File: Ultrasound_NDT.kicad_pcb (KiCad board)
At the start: 6 copper layers, 100 x 100 mm, 316 parts, among them J1 Conn_01x02_Pin, J10 CONSMA002-SMD, J11 Logger Connector, J12 UART Connector, J13 External UART, J14 External I2C, J15 JTAG Header, J16 Conn_02x04_Odd_Even, J17 Input Power, J18 Conn_01x02_Pin, J19 Conn_01x02_Pin, J2 Conn_01x02_Pin, J20 Conn_01x02_Pin, J21 Conn_01x02_Pin, J22 Conn_01x02_Pin, J23 Conn_01x02_Pin, J24 Conn_01x02_Pin, J25 Conn_01x02_Pin, J26 Spectrography Power, J27 Conn_01x02_Pin, J28 Conn_02x04_Odd_Even, J3 CONSMA002-SMD, J4 CONSMA002-SMD, J5 CONSMA002-SMD, J6 CONSMA002-SMD, J7 CONSMA002-SMD, J8 CONSMA002-SMD, J9 CONSMA002-SMD, SW1 XRSn_button, U1 AD8334ACPZ, U10 TLV9354IDR, U11 TLV9354IDR, U12 TPS63700DRCR, U13 M24M01E-FMN6TP, U14 LDL212PU50R, U15 AZ1117CH2-3.3, U16 AZ1117CH2-3.3, U17 TRS3221EIPWR, U2 DSC1001DI2-125.0000T, U3 MAX14808ETK_, U4 AD8334ACPZ, U5 F280025PNS, U6 REF3030, U7 MIC920YC5-TR, U8 TLV9354IDR, U9 TLV9354IDR, Y2 H130B-16.000-18-3030-EXT-TR

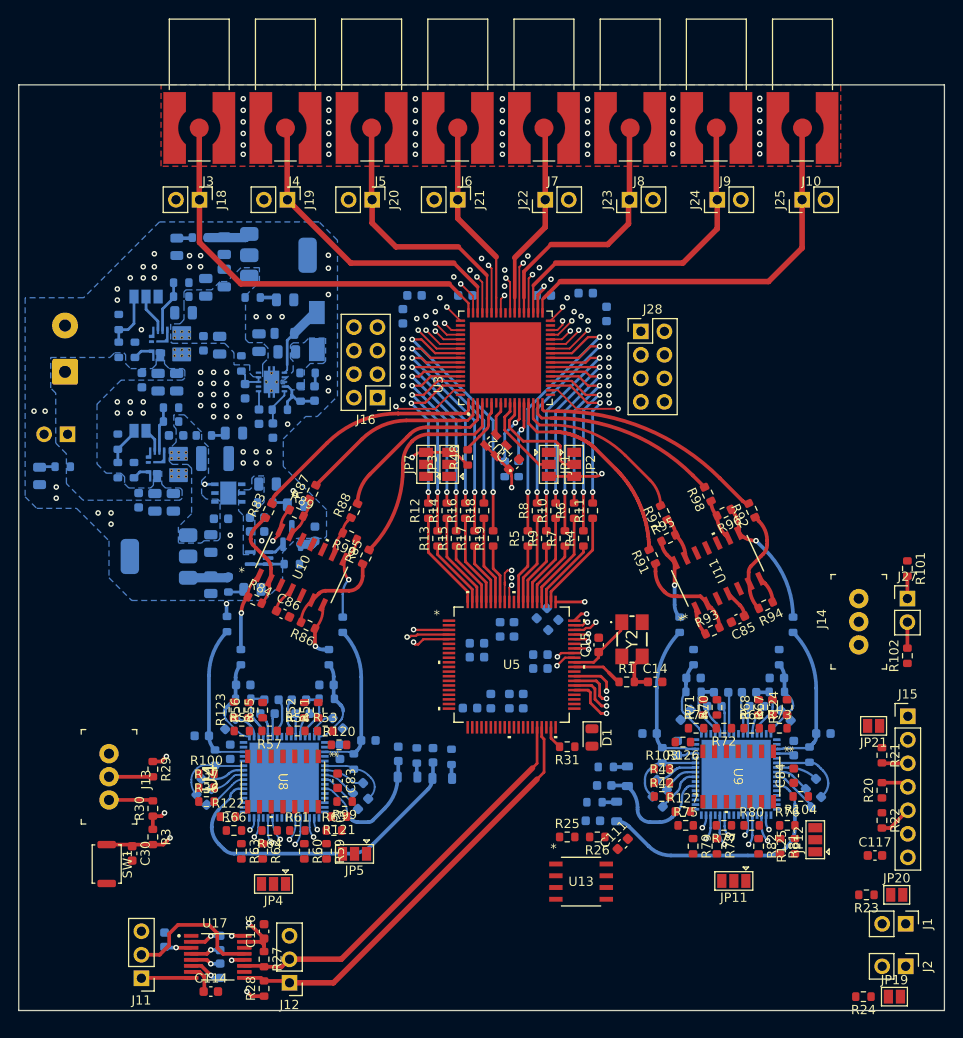
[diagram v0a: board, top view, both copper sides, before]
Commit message: Finished 70% fr this time, power planes are remaining and some minor connections to the AFE's power & cfg pins, dont forget xrst
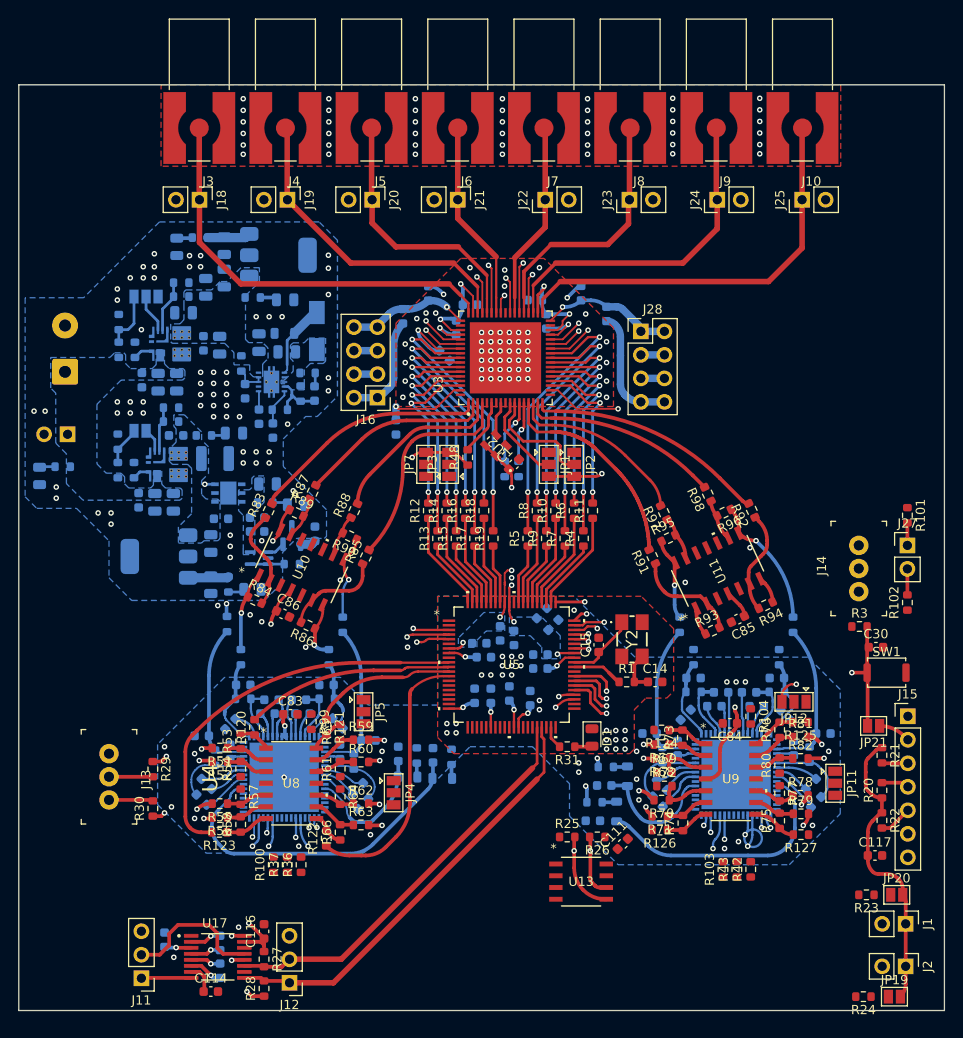
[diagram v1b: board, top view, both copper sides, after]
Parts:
- moved SW1 86.7 mm to (153.5, 98.2), turned to 0 degrees
- moved C30 83.4 mm to (152.3, 95.5), turned to 0 degrees
- moved R3 79.7 mm to (150.6, 93.3), turned to 0 degrees
- moved JP4 16.3 mm to (100.2, 111.2), turned to -90 degrees
- moved JP5 15.4 mm to (97.0, 102.5), turned to -90 degrees
- moved JP11 15.2 mm to (147.9, 110.2), turned to -90 degrees
- moved JP12 15.1 mm to (143.5, 101.4), turned to 180 degrees
- moved R124 13.8 mm to (129.2, 104.5), turned to 180 degrees
- moved R125 13.4 mm to (144.2, 103.6), turned to 180 degrees
- moved R123 13.3 mm to (81.4, 115.5), turned to 180 degrees
- moved R63 13.2 mm to (96.7, 114.7), turned to 0 degrees
- moved R127 13.0 mm to (144.2, 115.8), turned to 180 degrees
- moved R103 12.7 mm to (135.8, 119.5), turned to 90 degrees
- moved R71 12.6 mm to (129.0, 113.8), turned to 180 degrees
- moved R67 12.6 mm to (129.2, 106.0), turned to 180 degrees
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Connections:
- C37 pad 1: /Receiving Section/TR_OUT2 -> /Receiving Section/TR_OUT4
- R120 pad 2: /Main MCU Section/ADC1 -> /Main MCU Section/ADC2
- R123 pad 2: /Main MCU Section/ADC2 -> /Main MCU Section/ADC1
- R130 pad 2: /Receiving Section/TR_OUT2 -> /Receiving Section/TR_OUT4
- R33 pad 1: /Receiving Section/TR_OUT2 -> /Receiving Section/TR_OUT4
- R51 pad 2: /Receiving Section/ADC1_L -> /Receiving Section/ADC2_L
- R52 pad 2: /Receiving Section/ADC1_H -> /Receiving Section/ADC2_H
- R55 pad 2: /Receiving Section/ADC2_H -> /Receiving Section/ADC1_H
- R56 pad 2: /Receiving Section/ADC2_L -> /Receiving Section/ADC1_L
- U4 pad 16: /Receiving Section/TR_OUT2 -> /Receiving Section/TR_OUT4
- U5 pad 10: /Main MCU Section/ADC3 -> /Main MCU Section/ADC1
- U5 pad 12: /Main MCU Section/ADC1 -> /Main MCU Section/ADC4
- U5 pad 13: /Main MCU Section/ADC4 -> /Main MCU Section/ADC3
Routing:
- net /Main MCU Section/RS232_FOFF: track 61.8 -> 3.00 mm
- net /Main MCU Section/ADC1: track 0.00 -> 42.6 mm
- net MCU_IO_3V3: track 31.3 -> 72.4 mm, vias 7 -> 11
- net /Main MCU Section/XRSn: track 46.5 -> 15.6 mm
- net /Main MCU Section/ADC3: track 0.00 -> 28.6 mm
- net /Main MCU Section/I2CA_SDA: track 0.00 -> 26.9 mm, vias 0 -> 2
- net /Main MCU Section/I2CA_SCL: track 0.00 -> 26.1 mm, vias 0 -> 2
- net /Main MCU Section/ADC2: track 0.00 -> 22.6 mm
- net /Main MCU Section/AFE_GAIN_B2: track 2.68 -> 21.9 mm, vias 1 -> 2
- net /Main MCU Section/AFE_GAIN_B1: track 1.57 -> 19.2 mm, vias 1 -> 2
- net +5V: track 5.87 -> 22.7 mm, vias 0 -> 4
- net /Main MCU Section/ADC4: track 0.00 -> 15.5 mm
- net VGNB: track 2.52 -> 17.1 mm
- net /Receiving Section/ADC4_L: track 2.16 -> 16.4 mm, vias 1 -> 2
- net /Receiving Section/ADC2_H: track 2.52 -> 16.8 mm, vias 1 -> 2
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- added copper zone on In4.Cu, net GND
- added copper zone on B.Cu, net MCU_1V2
- added copper zone on B.Cu, net MCU_IO_3V3

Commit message: 1/4 AFE edits left to go, check if MCU ADC channels could be swapped (use oth ADCs), add voltage monitoring & power planes
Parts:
- moved JP4 15.1 mm to (88.1, 120.2), turned to 180 degrees
- moved JP11 11.7 mm to (142.1, 120.2), turned to 180 degrees
- moved R100 10.5 mm to (76.7, 119.0)
- moved R36 10.5 mm to (79.7, 119.0)
- moved R37 10.5 mm to (78.2, 119.0)
- moved C4 4.68 mm to (119.2, 63.0), turned to -90 degrees
- moved C78 2.22 mm to (146.5, 110.1), turned to -90 degrees
- moved C75 1.84 mm to (128.0, 110.5), turned to -90 degrees
- moved C42 1.40 mm to (97.8, 111.3), turned to -90 degrees
- moved R62 1.33 mm to (97.7, 111.5)
- moved R64 0.99 mm to (95.4, 112.0)
- moved C66 0.92 mm to (146.7, 103.9)
- moved C82 0.84 mm to (145.0, 109.5), turned to -90 degrees
- moved C57 0.83 mm to (127.9, 104.0)
- moved C84 0.77 mm to (136.6, 103.0)
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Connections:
- C63 pad 1: /Receiving Section/TR_OUT6 -> /Receiving Section/TR_OUT8
- R128 pad 2: /Receiving Section/TR_OUT6 -> /Receiving Section/TR_OUT8
- R45 pad 1: /Receiving Section/TR_OUT6 -> /Receiving Section/TR_OUT8
- U1 pad 16: /Receiving Section/TR_OUT6 -> /Receiving Section/TR_OUT8
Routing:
- net +5V: track 22.7 -> 38.1 mm, vias 4 -> 10
- net /Receiving Section/ADC2_H: track 16.8 -> 4.77 mm
- net /Receiving Section/ADC2_L: track 14.6 -> 2.78 mm
- net /Receiving Section/MODE_B: track 0.00 -> 9.13 mm, vias 0 -> 1
- net /Receiving Section/TR_OUT6: track 25.7 -> 16.6 mm
- net /Receiving Section/TR_OUT8: track 0.00 -> 8.84 mm
- net /Receiving Section/ADC1_H: track 11.1 -> 3.97 mm
- net /Receiving Section/MODE_A: track 0.00 -> 6.49 mm, vias 0 -> 1
- net /Receiving Section/ADC1_L: track 10.5 -> 4.15 mm
- net Net-(U9-+IN_B): track 5.78 -> 0.00 mm
- net /Receiving Section/ADC8_L: track 14.5 -> 18.8 mm
- net /Receiving Section/HILO_B: track 0.00 -> 3.80 mm, vias 0 -> 1
- net Net-(U1-LMD3): track 0.00 -> 3.17 mm
- net /Receiving Section/HILO_A: track 0.00 -> 3.04 mm, vias 0 -> 1
- net /Receiving Section/LNAA8_N: track 8.55 -> 6.11 mm
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
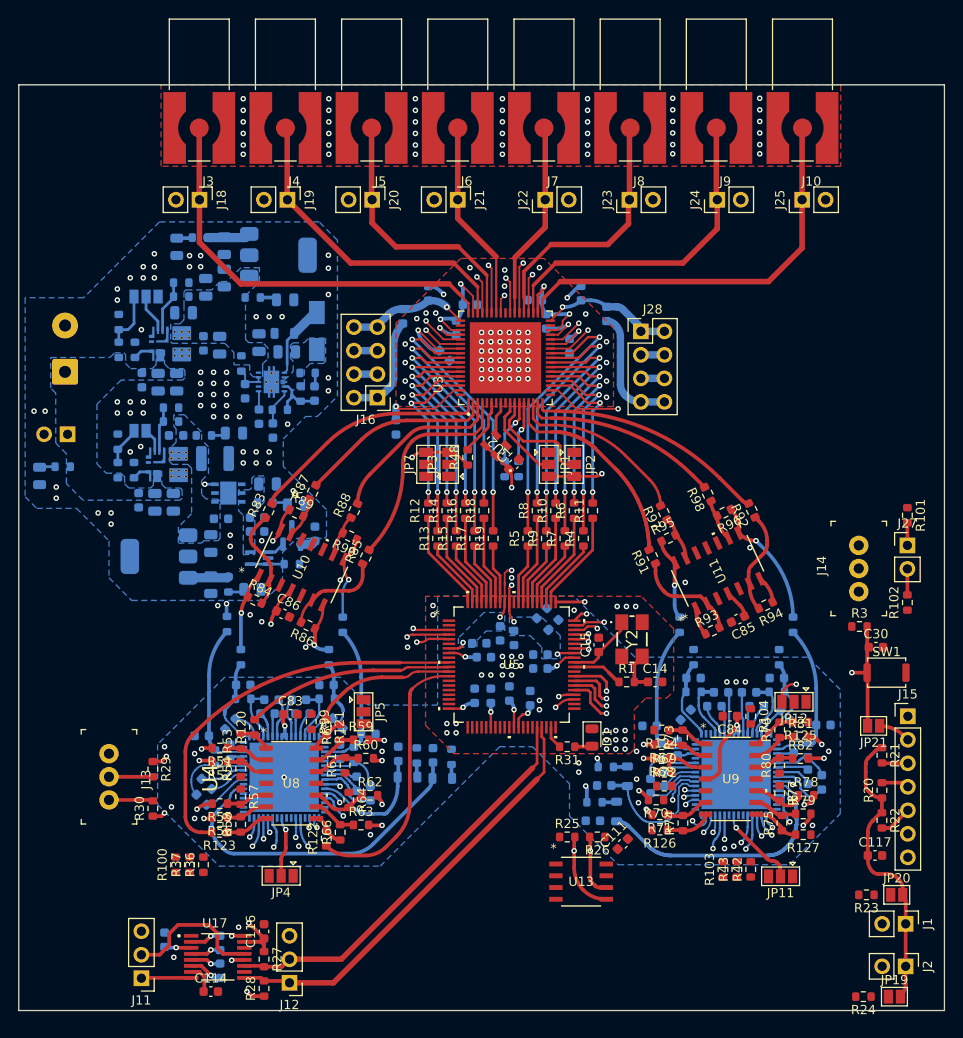
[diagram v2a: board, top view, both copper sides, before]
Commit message: 5% left, rearrange ADC channels for right AFE
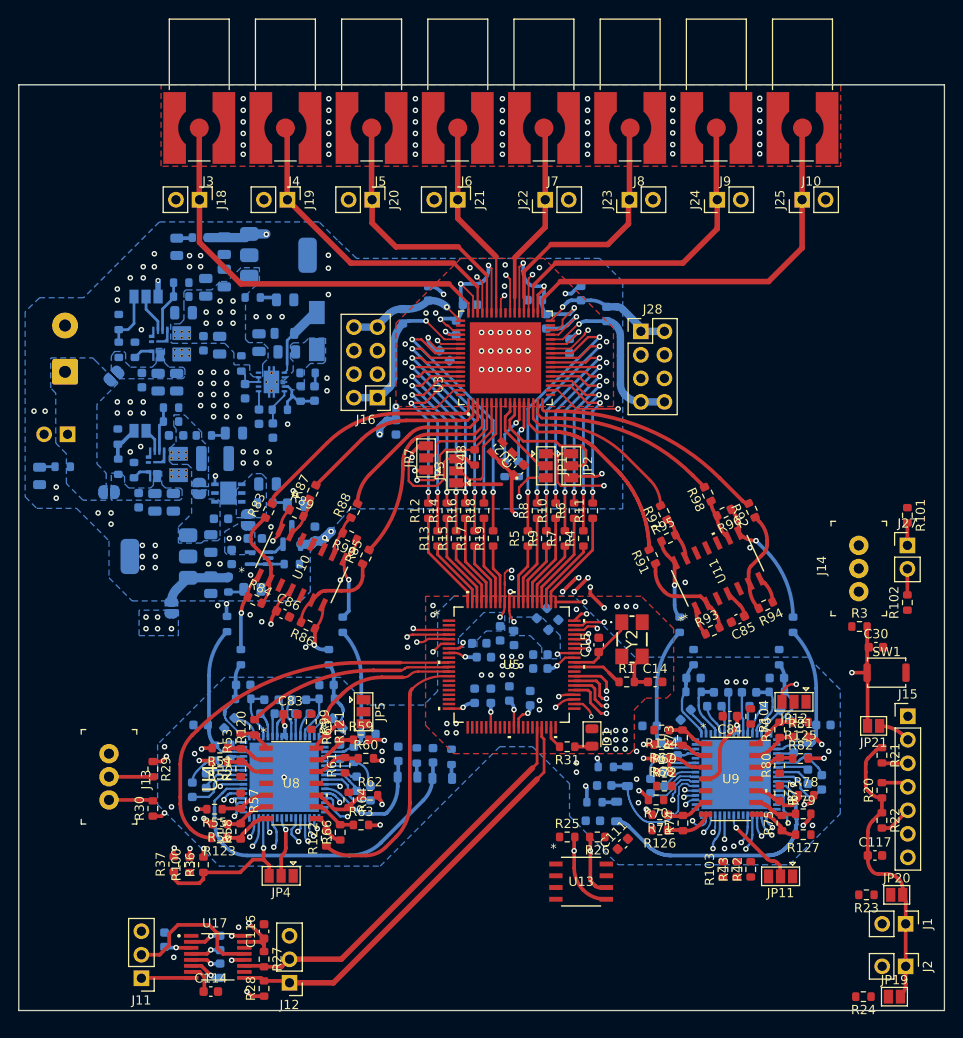
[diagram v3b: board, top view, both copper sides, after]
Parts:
- added JP10: SolderJumper_2_Open, Jumper:SolderJumper-2_P1.3mm_Open_RoundedPad1.0x1.5mm, B.Cu at (76.2, 91.2)
- added JP13: SolderJumper_2_Open, Jumper:SolderJumper-2_P1.3mm_Open_RoundedPad1.0x1.5mm, B.Cu at (84.5, 81.8)
- added JP6: SolderJumper_2_Open, Jumper:SolderJumper-2_P1.3mm_Open_RoundedPad1.0x1.5mm, B.Cu at (70.0, 66.2)
- added JP8: SolderJumper_2_Open, Jumper:SolderJumper-2_P1.3mm_Open_RoundedPad1.0x1.5mm, B.Cu at (69.5, 78.8)
- added JP9: SolderJumper_2_Open, Jumper:SolderJumper-2_P1.3mm_Open_RoundedPad1.0x1.5mm, B.Cu at (79.2, 78.3)
- moved C27 3.89 mm to (82.8, 85.8), turned to -90 degrees
- moved C28 2.26 mm to (85.2, 83.8)
- moved R37 1.70 mm to (76.5, 119.0)
- moved R100 1.50 mm to (78.2, 119.0)
- moved C39 1.47 mm to (78.5, 110.9), turned to -90 degrees
- moved C35 1.18 mm to (79.4, 103.9)
- moved U2 1.06 mm to (112.0, 74.5)
- moved JP3 1.03 mm to (107.0, 76.5)
- moved R55 0.83 mm to (80.9, 113.0)
- moved C1 0.79 mm to (113.8, 76.4)
- moved R48 0.75 mm to (109.0, 75.0)
- moved R58 0.75 mm to (83.7, 115.4)
- moved JP7 0.70 mm to (103.8, 75.0)
- moved R56 0.70 mm to (81.5, 114.6)
- moved R123 0.60 mm to (81.4, 116.1)
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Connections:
- C27 pad 1: +5V -> +5V_VFD
- C28 pad 1: +5V -> +5V_VFD
- C83 pad 1: +5V -> +5V_VFD
- C84 pad 1: +5V -> +5V_VFD
- C85 pad 1: +5V -> +5V_VFD
- C86 pad 1: +5V -> +5V_VFD
- C88 pad 1: +12V -> +12V_VFD
- C89 pad 1: +12V -> +12V_VFD
- C91 pad 1: +12V -> +12V_VFD
- C92 pad 1: +7V -> +7V_VFD
- C93 pad 1: MCU_IO_3V3 -> +3.3V
- C94 pad 1: +7V -> +7V_VFD
- C96 pad 1: +12V -> +12V_VFD
- C97 pad 1: +12V -> +12V_VFD
- C98 pad 1: +12V -> +12V_VFD
- JP11 pad 3: +5V -> +5V_VFD
- JP12 pad 3: +5V -> +5V_VFD
- JP4 pad 3: +5V -> +5V_VFD
- JP5 pad 3: +5V -> +5V_VFD
- PS1 pad 6: +12V -> +12V_VFD
- PS3 pad 6: +12V -> +12V_VFD
- R108 pad 1: +12V -> +12V_VFD
- R111 pad 1: +12V -> +12V_VFD
- R121 pad 1: /Main MCU Section/ADC4 -> /Main MCU Section/ADC3
- R122 pad 1: /Main MCU Section/ADC3 -> /Main MCU Section/ADC4
- R139 pad 1: MCU_IO_3V3 -> +3.3V
- R36 pad 1: +5V -> +5V_VFD
- R37 pad 1: +5V -> +5V_VFD
- R42 pad 1: +5V -> +5V_VFD
- R43 pad 1: +5V -> +5V_VFD
- R59 pad 2: /Receiving Section/ADC4_L -> /Receiving Section/ADC3_L
- R60 pad 2: /Receiving Section/ADC4_H -> /Receiving Section/ADC3_H
- R62 pad 2: /Receiving Section/ADC3_H -> /Receiving Section/ADC4_H
- R63 pad 2: /Receiving Section/ADC3_L -> /Receiving Section/ADC4_L
- U1 pad 26: +5V -> +5V_VFD
- U1 pad 36: +5V -> +5V_VFD
- U1 pad 45: +5V -> +5V_VFD
- U1 pad 55: +5V -> +5V_VFD
- U1 pad 8: +5V -> +5V_VFD
- U1 pad 9: +5V -> +5V_VFD
- U10 pad 4: +5V -> +5V_VFD
- U11 pad 4: +5V -> +5V_VFD
- U14 pad 4: +7V -> +7V_VFD
- U15 pad 1: +7V -> +7V_VFD
- U15 pad 3: MCU_IO_3V3 -> +3.3V
- U4 pad 26: +5V -> +5V_VFD
- U4 pad 36: +5V -> +5V_VFD
- U4 pad 45: +5V -> +5V_VFD
- U4 pad 55: +5V -> +5V_VFD
- U4 pad 8: +5V -> +5V_VFD
- U4 pad 9: +5V -> +5V_VFD
- U5 pad 12: /Main MCU Section/ADC4 -> /Main MCU Section/ADC3
- U5 pad 13: /Main MCU Section/ADC3 -> /Main MCU Section/ADC4
- U5 pad 54: /Main MCU Section/RS232_FOFF -> /Main MCU Section/RS232_FON
- U5 pad 56: /Main MCU Section/MODE1 -> /Main MCU Section/MODE0
- U5 pad 57: /Main MCU Section/MODE0 -> /Main MCU Section/MODE1
- U5 pad 6: /Main MCU Section/RS232_FON -> /Main MCU Section/RS232_FOFF
- U7 pad 5: +5V -> +5V_VFD
- U8 pad 4: +5V -> +5V_VFD
- U9 pad 4: +5V -> +5V_VFD
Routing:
- net /Main MCU Section/RS232_FON: track 1.39 -> 61.6 mm, vias 1 -> 2
- net +5V_VFD: track 0.00 -> 59.8 mm, vias 0 -> 14
- net +5V_PULSE: track 13.7 -> 69.4 mm, vias 2 -> 10
- net /Main MCU Section/XRSn: track 15.6 -> 69.6 mm, vias 2 -> 4
- net /Main MCU Section/RS232_FOFF: track 3.00 -> 49.8 mm
- net +3.3V_PULSE: track 34.7 -> 79.8 mm, vias 4 -> 7
- net +5V: track 38.1 -> 0.00 mm, vias 10 -> 0
- net /Main MCU Section/MODE0: track 8.54 -> 41.7 mm, vias 2 -> 4
- net /Main MCU Section/MODE1: track 8.21 -> 39.2 mm, vias 2 -> 4
- net GND: track 3.92 -> 21.1 mm, vias 221 -> 206
- net VPPB: track 20.0 -> 35.1 mm
- net /Receiving Section/EN12_A: track 0.00 -> 14.4 mm, vias 0 -> 2
- net /Receiving Section/EN34_A: track 0.00 -> 13.8 mm, vias 0 -> 2
- net -5V_PULSE: track 9.31 -> 23.0 mm
- net /Receiving Section/CLAMP12_A: track 0.00 -> 13.1 mm, vias 0 -> 2
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- added copper zone on B.Cu, net +12V_VFD
- added copper zone on In3.Cu, net +3.3V_PULSE
- added copper zone on B.Cu, net +5V_VFD
- added copper zone on In3.Cu, net +5V_VFD
- added copper zone on B.Cu, net +7V_VFD
- added copper zone on In2.Cu, net MCU_1V2
- added copper zone on In3.Cu, net MCU_IO_3V3
- added copper zone on In3.Cu, net VNNA
- added copper zone on In3.Cu, net VNNB
